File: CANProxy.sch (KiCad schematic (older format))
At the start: 2 parts

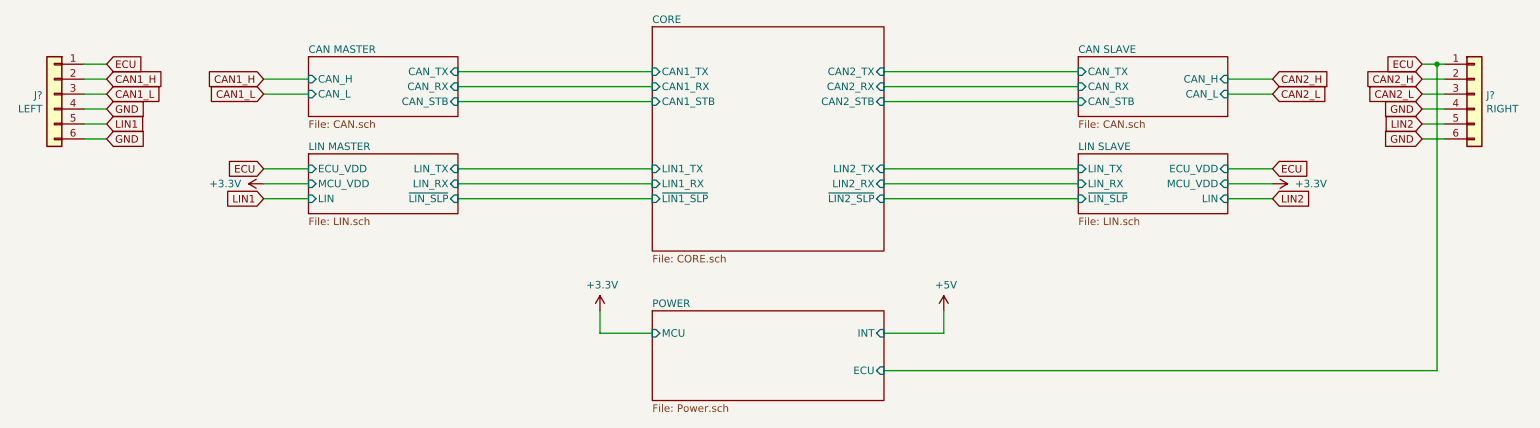
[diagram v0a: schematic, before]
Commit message: corrected CAN schematic
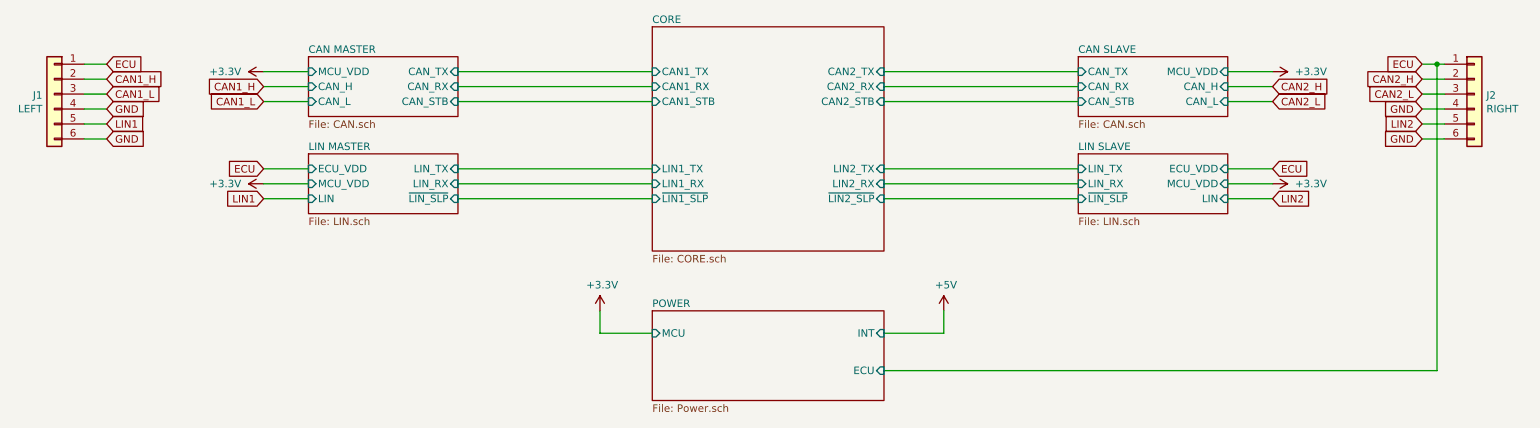
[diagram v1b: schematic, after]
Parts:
- J1, J2: renamed from J?; footprint (none) -> Connector_Wago:Wago_734-166_1x06_P3.50mm_Horizontal; Description (none) -> Pluggable male terminal block, 6-ways. R/A pin header, pitc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; Manufacturer (none) -> CIXI ULO ELECTRONICS CO.,LTD; Mount (none) -> DO NOT MOUNT; MountType (none) -> TH; PartNumber (none) -> ULO-TB01-15RC/3.5-06P-4
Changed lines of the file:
@@
 F3 "CAN_RX" I R 3800 2400 50
 F4 "CAN_STB" I R 3800 2500 50
-F5 "CAN_H" I L 2800 2350 50
-F6 "CAN_L" I L 2800 2450 50
+F5 "CAN_H" I L 2800 2400 50
+F6 "CAN_L" I L 2800 2500 50
+F7 "MCU_VDD" I L 2800 2300 50
 $EndSheet
 $Sheet
@@
 F3 "CAN_RX" I L 7950 2400 50
 F4 "CAN_STB" I L 7950 2500 50
-F5 "CAN_H" I R 8950 2350 50
-F6 "CAN_L" I R 8950 2450 50
+F5 "CAN_H" I R 8950 2400 50
+F6 "CAN_L" I R 8950 2500 50
+F7 "MCU_VDD" I R 8950 2300 50
 $EndSheet
 Text GLabel 1450 2250 2    50   Input ~ 0
@@
 GND
 $Comp
-L Connector_Generic:Conn_01x06 J?
+L Connector_Generic:Conn_01x06 J1
 U 1 1 600FD9BD
 P 1100 2450
-F 0 "J?" H 1180 2442 50  0000 L CNN
+F 0 "J1" H 1180 2442 50  0000 L CNN
 F 1 "LEFT" H 1180 2351 50  0000 L CNN
-F 2 "" H 1100 2450 50  0001 C CNN
+F 2 "Connector_Wago:Wago_734-166_1x06_P3.50mm_Horizontal" H 1100 2450 50  0001 C CNN
 F 3 "~" H 1100 2450 50  0001 C CNN
+F 4 "DO NOT MOUNT" H 1100 2450 50  0001 C CNN "Mount"
+F 5 "TH" H 1100 2450 50  0001 C CNN "MountType"
+F 6 "CIXI ULO ELECTRONICS CO.,LTD" H 1100 2450 50  0001 C CNN "Manufacturer"
+F 7 "Pluggable male terminal block, 6-ways. R/A pin header, pitch 3.50mm, closed type" H 1100 2450 50  0001 C CNN "Description"
+F 8 "ULO-TB01-15RC/3.5-06P-4" H 1100 2450 50  0001 C CNN "PartNumber"
 	1    1100 2450
 	-1   0    0    -1
@@
 GND
 $Comp
-L Connector_Generic:Conn_01x06 J?
+L Connector_Generic:Conn_01x06 J2
 U 1 1 600FEB50
 P 10600 2450
-F 0 "J?" H 10680 2442 50  0000 L CNN
+F 0 "J2" H 10680 2442 50  0000 L CNN
 F 1 "RIGHT" H 10680 2351 50  0000 L CNN
-F 2 "" H 10600 2450 50  0001 C CNN
+F 2 "Connector_Wago:Wago_734-166_1x06_P3.50mm_Horizontal" H 10600 2450 50  0001 C CNN
 F 3 "~" H 10600 2450 50  0001 C CNN
+F 4 "DO NOT MOUNT" H 10600 2450 50  0001 C CNN "Mount"
+F 5 "TH" H 10600 2450 50  0001 C CNN "MountType"
+F 6 "CIXI ULO ELECTRONICS CO.,LTD" H 10600 2450 50  0001 C CNN "Manufacturer"
+F 7 "Pluggable male terminal block, 6-ways. R/A pin header, pitch 3.50mm, closed type" H 10600 2450 50  0001 C CNN "Description"
+F 8 "ULO-TB01-15RC/3.5-06P-4" H 10600 2450 50  0001 C CNN "PartNumber"
 	1    10600 2450
 	1    0    0    -1
@@
 Wire Wire Line
 	10400 2750 10250 2750
-Text GLabel 2500 2350 0    50   Input ~ 0
+Text GLabel 2500 2400 0    50   Input ~ 0
 CAN1_H
-Text GLabel 2500 2450 0    50   Input ~ 0
+Text GLabel 2500 2500 0    50   Input ~ 0
 CAN1_L
-Text GLabel 9250 2350 2    50   Input ~ 0
+Text GLabel 9250 2400 2    50   Input ~ 0
 CAN2_H
-Text GLabel 9250 2450 2    50   Input ~ 0
+Text GLabel 9250 2500 2    50   Input ~ 0
 CAN2_L
 Wire Wire Line
-	8950 2350 9250 2350
-Wire Wire Line
-	9250 2450 8950 2450
-Wire Wire Line
-	2800 2450 2500 2450
-Wire Wire Line
-	2500 2350 2800 2350
+	8950 2400 9250 2400
+Wire Wire Line
+	9250 2500 8950 2500
+Wire Wire Line
+	2800 2500 2500 2500
+Wire Wire Line
+	2500 2400 2800 2400
 Text GLabel 2500 2950 0    50   Input ~ 0
 ECU
@@
 	10350 2250 10400 2250
 $Comp
-L power:+3.3V #PWR?
+L power:+3.3V #PWR03
 U 1 1 600C2E43
 P 4750 3900
-F 0 "#PWR?" H 4750 3750 50  0001 C CNN
+F 0 "#PWR03" H 4750 3750 50  0001 C CNN
 F 1 "+3.3V" H 4765 4073 50  0000 C CNN
 F 2 "" H 4750 3900 50  0001 C CNN
@@
 	2500 3050 2800 3050
 $Comp
-L power:+3.3V #PWR?
+L power:+3.3V #PWR02
 U 1 1 600C3531
 P 2500 3050
-F 0 "#PWR?" H 2500 2900 50  0001 C CNN
+F 0 "#PWR02" H 2500 2900 50  0001 C CNN
 F 1 "+3.3V" V 2500 3200 50  0000 L CNN
 F 2 "" H 2500 3050 50  0001 C CNN
@@
 $EndComp
 $Comp
-L power:+3.3V #PWR?
+L power:+3.3V #PWR06
 U 1 1 600C429C
 P 9250 3050
-F 0 "#PWR?" H 9250 2900 50  0001 C CNN
+F 0 "#PWR06" H 9250 2900 50  0001 C CNN
 F 1 "+3.3V" V 9250 3200 50  0000 L CNN
 F 2 "" H 9250 3050 50  0001 C CNN
@@
 $EndComp
 $Comp
-L power:+5V #PWR?
+L power:+5V #PWR04
 U 1 1 600C5629
 P 7050 3900
-F 0 "#PWR?" H 7050 3750 50  0001 C CNN
+F 0 "#PWR04" H 7050 3750 50  0001 C CNN
 F 1 "+5V" H 7065 4073 50  0000 C CNN
 F 2 "" H 7050 3900 50  0001 C CNN
@@
 Wire Wire Line
 	5100 3150 3800 3150
+$Comp
+L power:+3.3V #PWR05
+U 1 1 6010BBA6
+P 9250 2300
+F 0 "#PWR05" H 9250 2150 50  0001 C CNN
+F 1 "+3.3V" V 9250 2450 50  0000 L CNN
+F 2 "" H 9250 2300 50  0001 C CNN
+F 3 "" H 9250 2300 50  0001 C CNN
+	1    9250 2300
+	0    1    1    0
+$EndComp
+Wire Wire Line
+	9250 2300 8950 2300
+$Comp
+L power:+3.3V #PWR01
+U 1 1 6010D180
+P 2500 2300
+F 0 "#PWR01" H 2500 2150 50  0001 C CNN
+F 1 "+3.3V" V 2500 2450 50  0000 L CNN
+F 2 "" H 2500 2300 50  0001 C CNN
+F 3 "" H 2500 2300 50  0001 C CNN
+	1    2500 2300
+	0    -1   -1   0
+$EndComp
+Wire Wire Line
+	2500 2300 2800 2300
 $EndSCHEMATC

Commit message: CAN part routing
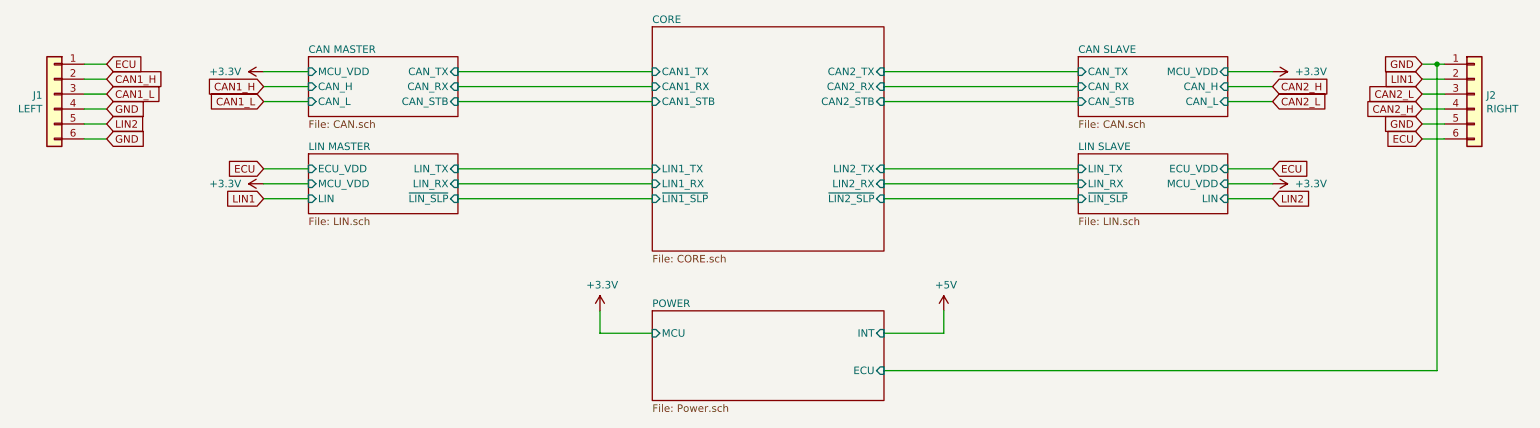
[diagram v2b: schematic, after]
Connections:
- net CAN2_H: now also J2.4 (Pin_4); no longer J2.2 (Pin_2)
- net ECU: now also J2.6 (Pin_6); no longer J2.1 (Pin_1)
- net GND: now also J2.1 (Pin_1), J2.5 (Pin_5); no longer J2.4 (Pin_4), J2.6 (Pin_6)
- net LIN1: now also J2.2 (Pin_2); no longer J1.5 (Pin_5)
- net LIN2: now also J1.5 (Pin_5); no longer J2.5 (Pin_5)
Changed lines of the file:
@@
 Text GLabel 1450 2450 2    50   Input ~ 0
 CAN1_L
-Text GLabel 1450 2650 2    50   Input ~ 0
+Text GLabel 10250 2350 0    50   Input ~ 0
 LIN1
 Text GLabel 1450 2750 2    50   Input ~ 0
@@
 	1300 2550 1450 2550
 Wire Wire Line
-	1450 2650 1300 2650
+	10250 2350 10400 2350
 Wire Wire Line
 	1300 2750 1450 2750
-Text GLabel 10250 2250 0    50   Input ~ 0
+Text GLabel 10250 2750 0    50   Input ~ 0
 ECU
-Text GLabel 10250 2350 0    50   Input ~ 0
+Text GLabel 10250 2550 0    50   Input ~ 0
 CAN2_H
 Text GLabel 10250 2450 0    50   Input ~ 0
 CAN2_L
+Text GLabel 1450 2650 2    50   Input ~ 0
+LIN2
+Text GLabel 10250 2250 0    50   Input ~ 0
+GND
 Text GLabel 10250 2650 0    50   Input ~ 0
-LIN2
-Text GLabel 10250 2750 0    50   Input ~ 0
-GND
-Text GLabel 10250 2550 0    50   Input ~ 0
 GND
 $Comp
@@
 	10250 2250 10350 2250
 Wire Wire Line
-	10400 2350 10250 2350
+	10400 2450 10250 2450
 Wire Wire Line
-	10250 2450 10400 2450
+	10250 2550 10400 2550
 Wire Wire Line
-	10400 2550 10250 2550
+	10400 2650 10250 2650
 Wire Wire Line
-	10250 2650 10400 2650
+	1450 2650 1300 2650
 Wire Wire Line
 	10400 2750 10250 2750
